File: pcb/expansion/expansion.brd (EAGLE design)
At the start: 88 x 42 mm, 53 parts, among them IC3 STM32F042F4, J1 AUDIO_JACK_3.5MM_PTH, J2 AUDIO_JACK_3.5MM_PTH, J3 AUDIO_JACK_3.5MM_PTH, J4 AUDIO_JACK_3.5MM_PTH, J5 AUDIO_JACK_3.5MM_PTH, J6 AUDIO_JACK_3.5MM_PTH, SW3 324_SW, SW4 324_SW, U1 USBC_16P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

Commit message: forgot to connect a gnd pin
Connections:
- net N$3 renamed CH1
- net N$4 renamed CH2
- net N$6 renamed CH3
- net N$7 renamed CH4
- net N$8 renamed CH5
- net N$9 renamed CH6
- net GND: now also J5.SLEEVE
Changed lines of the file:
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@@
 <grid distance="5" unitdist="mil" unit="mil" style="lines" multiple="1" display="no" altdistance="1" altunitdist="mil" altunit="mil"/>
 <layers>
-<layer number="1" name="Top" color="4" fill="1" visible="no" active="yes"/>
+<layer number="1" name="Top" color="4" fill="1" visible="yes" active="yes"/>
 <layer number="2" name="Route2" color="16" fill="1" visible="no" active="no"/>
 <layer number="3" name="Route3" color="17" fill="1" visible="no" active="no"/>
@@
 <layer number="19" name="Unrouted" color="6" fill="1" visible="yes" active="yes"/>
 <layer number="20" name="Dimension" color="24" fill="1" visible="yes" active="yes"/>
-<layer number="21" name="tPlace" color="7" fill="1" visible="no" active="yes"/>
+<layer number="21" name="tPlace" color="7" fill="1" visible="yes" active="yes"/>
 <layer number="22" name="bPlace" color="7" fill="1" visible="yes" active="yes"/>
-<layer number="23" name="tOrigins" color="15" fill="1" visible="no" active="yes"/>
+<layer number="23" name="tOrigins" color="15" fill="1" visible="yes" active="yes"/>
 <layer number="24" name="bOrigins" color="15" fill="1" visible="yes" active="yes"/>
-<layer number="25" name="tNames" color="7" fill="1" visible="no" active="yes"/>
+<layer number="25" name="tNames" color="7" fill="1" visible="yes" active="yes"/>
 <layer number="26" name="bNames" color="7" fill="1" visible="yes" active="yes"/>
-<layer number="27" name="tValues" color="7" fill="1" visible="no" active="yes"/>
-<layer number="28" name="bValues" color="7" fill="1" visible="no" active="yes"/>
+<layer number="27" name="tValues" color="7" fill="1" visible="yes" active="yes"/>
+<layer number="28" name="bValues" color="7" fill="1" visible="yes" active="yes"/>
 <layer number="29" name="tStop" color="7" fill="3" visible="no" active="yes"/>
 <layer number="30" name="bStop" color="7" fill="6" visible="no" active="yes"/>
@@
 <layer number="37" name="tTest" color="7" fill="1" visible="no" active="yes"/>
 <layer number="38" name="bTest" color="7" fill="1" visible="no" active="yes"/>
-<layer number="39" name="tKeepout" color="4" fill="11" visible="no" active="yes"/>
+<layer number="39" name="tKeepout" color="4" fill="11" visible="yes" active="yes"/>
 <layer number="40" name="bKeepout" color="1" fill="11" visible="yes" active="yes"/>
-<layer number="41" name="tRestrict" color="4" fill="10" visible="no" active="yes"/>
+<layer number="41" name="tRestrict" color="4" fill="10" visible="yes" active="yes"/>
 <layer number="42" name="bRestrict" color="1" fill="10" visible="yes" active="yes"/>
 <layer number="43" name="vRestrict" color="2" fill="10" visible="no" active="yes"/>
@@
 <layer number="49" name="Reference" color="7" fill="1" visible="no" active="yes"/>
 <layer number="50" name="dxf" color="7" fill="1" visible="no" active="no"/>
-<layer number="51" name="tDocu" color="7" fill="1" visible="no" active="yes"/>
+<layer number="51" name="tDocu" color="7" fill="1" visible="yes" active="yes"/>
 <layer number="52" name="bDocu" color="7" fill="1" visible="yes" active="yes"/>
 <layer number="53" name="tGND_GNDA" color="7" fill="1" visible="no" active="no"/>
@@
 <via x="28.194" y="23.876" extent="1-16" drill="0.5"/>
 <contactref element="R14" pad="1"/>
+<contactref element="J5" pad="SLEEVE"/>
+<wire x1="78.613" y1="28.575" x2="76.073" y2="38.227" width="0" layer="19" extent="1-1"/>
+<wire x1="81.6575" y1="25.32" x2="78.613" y2="28.575" width="0" layer="19" extent="1-1"/>
+<wire x1="80.7425" y1="24.225" x2="81.6575" y2="25.32" width="0" layer="19" extent="1-1"/>
+<wire x1="85.8375" y1="25.32" x2="81.6575" y2="25.32" width="0" layer="19" extent="1-1"/>
+<wire x1="83.693" y1="29.221" x2="81.6575" y2="25.32" width="0" layer="19" extent="1-1"/>
+<wire x1="80.7425" y1="17.775" x2="80.7425" y2="24.225" width="0" layer="19" extent="1-1"/>
+<wire x1="81.6575" y1="16.68" x2="80.7425" y2="17.775" width="0" layer="19" extent="1-1"/>
+<wire x1="85.8375" y1="16.68" x2="81.6575" y2="16.68" width="0" layer="19" extent="1-1"/>
+<wire x1="83.82" y1="12.054" x2="85.8375" y2="16.68" width="0" layer="19" extent="1-1"/>
+<wire x1="73.533" y1="13.462" x2="80.7425" y2="17.775" width="0" layer="19" extent="1-1"/>
+<wire x1="76.073" y1="3.683" x2="73.533" y2="13.462" width="0" layer="19" extent="1-1"/>
+<wire x1="61" y1="13.117" x2="73.533" y2="13.462" width="0" layer="19" extent="1-1"/>
+<wire x1="56.007" y1="15.61" x2="61" y2="13.117" width="0" layer="19" extent="1-1"/>
+<wire x1="48.387" y1="13.462" x2="56.007" y2="15.61" width="0" layer="19" extent="1-1"/>
+<wire x1="61" y1="4.917" x2="61" y2="13.117" width="0" layer="19" extent="1-1"/>
+<wire x1="53.127" y1="24.3152" x2="56.007" y2="15.61" width="0" layer="19" extent="1-1"/>
+<wire x1="53.467" y1="28.575" x2="53.127" y2="24.3152" width="0" layer="19" extent="1-1"/>
+<wire x1="48.727" y1="24.3152" x2="53.127" y2="24.3152" width="0" layer="19" extent="1-1"/>
+<wire x1="45.847" y1="22.479" x2="48.727" y2="24.3152" width="0" layer="19" extent="1-1"/>
+<wire x1="43.942" y1="22.617" x2="45.847" y2="22.479" width="0" layer="19" extent="1-1"/>
+<wire x1="61" y1="28.92" x2="53.467" y2="28.575" width="0" layer="19" extent="1-1"/>
+<wire x1="61" y1="37.12" x2="61" y2="28.92" width="0" layer="19" extent="1-1"/>
+<wire x1="35.1902" y1="21.445" x2="43.942" y2="22.617" width="0" layer="19" extent="1-1"/>
+<wire x1="32.385" y1="22.744" x2="35.1902" y2="21.445" width="0" layer="19" extent="1-1"/>
+<wire x1="28.194" y1="23.876" x2="32.385" y2="22.744" width="0" layer="19" extent="1-1"/>
+<wire x1="24.881" y1="25.527" x2="28.194" y2="23.876" width="0" layer="19" extent="1-1"/>
+<wire x1="28.321" y1="28.575" x2="24.881" y2="25.527" width="0" layer="19" extent="1-1"/>
+<wire x1="18.669" y1="23.357" x2="24.881" y2="25.527" width="0" layer="19" extent="1-1"/>
+<wire x1="15.986" y1="23.307" x2="18.669" y2="23.357" width="0" layer="19" extent="1-1"/>
+<wire x1="11.938" y1="23.357" x2="15.986" y2="23.307" width="0" layer="19" extent="1-1"/>
+<wire x1="8.1575" y1="24.225" x2="11.938" y2="23.357" width="0" layer="19" extent="1-1"/>
+<wire x1="7.2425" y1="25.32" x2="8.1575" y2="24.225" width="0" layer="19" extent="1-1"/>
+<wire x1="3.0625" y1="25.32" x2="7.2425" y2="25.32" width="0" layer="19" extent="1-1"/>
+<wire x1="5.08" y1="29.475" x2="3.0625" y2="25.32" width="0" layer="19" extent="1-1"/>
+<wire x1="10.708" y1="28.92" x2="7.2425" y2="25.32" width="0" layer="19" extent="1-1"/>
+<wire x1="8.1575" y1="17.775" x2="8.1575" y2="24.225" width="0" layer="19" extent="1-1"/>
+<wire x1="7.2425" y1="16.68" x2="8.1575" y2="17.775" width="0" layer="19" extent="1-1"/>
+<wire x1="3.0625" y1="16.68" x2="7.2425" y2="16.68" width="0" layer="19" extent="1-1"/>
+<wire x1="5.08" y1="12.562" x2="3.0625" y2="16.68" width="0" layer="19" extent="1-1"/>
+<wire x1="10.708" y1="13.117" x2="7.2425" y2="16.68" width="0" layer="19" extent="1-1"/>
+<wire x1="35.854" y1="28.92" x2="32.385" y2="22.744" width="0" layer="19" extent="1-1"/>
+<wire x1="35.854" y1="37.12" x2="35.854" y2="28.92" width="0" layer="19" extent="1-1"/>
+<wire x1="10.708" y1="37.12" x2="10.708" y2="28.92" width="0" layer="19" extent="1-1"/>
+<wire x1="10.708" y1="4.917" x2="10.708" y2="13.117" width="0" layer="19" extent="1-1"/>
+<wire x1="35.854" y1="13.117" x2="35.1902" y2="21.445" width="0" layer="19" extent="1-1"/>
+<wire x1="35.854" y1="4.917" x2="35.854" y2="13.117" width="0" layer="19" extent="1-1"/>
+<wire x1="43.434" y1="1.27" x2="35.854" y2="4.917" width="0" layer="19" extent="1-1"/>
+<wire x1="50.927" y1="3.683" x2="43.434" y2="1.27" width="0" layer="19" extent="1-1"/>
+<wire x1="50.927" y1="38.227" x2="53.467" y2="28.575" width="0" layer="19" extent="1-1"/>
+<wire x1="25.781" y1="38.227" x2="28.321" y2="28.575" width="0" layer="19" extent="1-1"/>
+<wire x1="25.781" y1="3.683" x2="35.854" y2="4.917" width="0" layer="19" extent="1-1"/>
+<wire x1="23.241" y1="13.462" x2="25.781" y2="3.683" width="0" layer="19" extent="1-1"/>
 </signal>
 <signal name="+3V3">
@@
 <wire x1="83.693" y1="23.368" x2="83.075" y2="22.75" width="0.2032" layer="1"/>
 </signal>
-<signal name="N$3">
+<signal name="CH1">
 <contactref element="J1" pad="TIP"/>
 <contactref element="JP1" pad="2"/>
@@
 <wire x1="36.449" y1="31.242" x2="25.781" y2="31.242" width="0.2032" layer="1"/>
 </signal>
-<signal name="N$4">
+<signal name="CH2">
 <contactref element="R8" pad="1"/>
 <contactref element="JP2" pad="2"/>
@@
 <wire x1="41.536" y1="29.602" x2="45.847" y2="29.602" width="0.2032" layer="1"/>
 </signal>
-<signal name="N$6">
+<signal name="CH3">
 <contactref element="R9" pad="1"/>
 <contactref element="JP3" pad="2"/>
@@
 <wire x1="66.519" y1="29.602" x2="66" y2="29.083" width="0.2032" layer="1"/>
 </signal>
-<signal name="N$7">
+<signal name="CH4">
 <contactref element="R10" pad="1"/>
 <contactref element="JP4" pad="2"/>
@@
 <wire x1="25.781" y1="11.176" x2="15.708" y2="11.176" width="0.2032" layer="1"/>
 </signal>
-<signal name="N$8">
+<signal name="CH5">
 <contactref element="R11" pad="1"/>
 <contactref element="JP5" pad="2"/>
@@
 <wire x1="40.854" y1="16.804" x2="40.8305" y2="16.8275" width="0.2032" layer="1"/>
 </signal>
-<signal name="N$9">
+<signal name="CH6">
 <contactref element="R12" pad="1"/>
 <contactref element="JP6" pad="2"/>

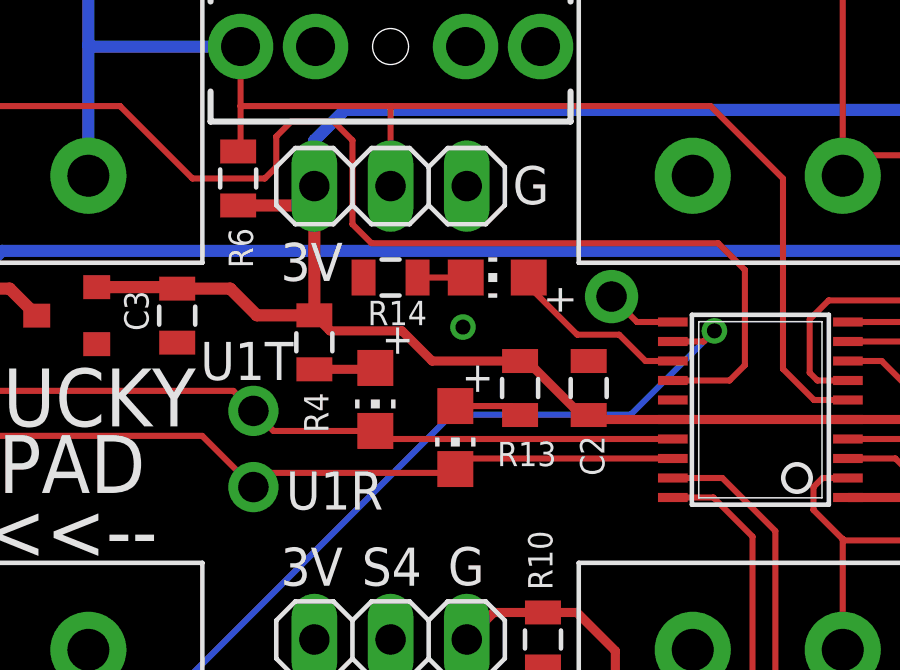
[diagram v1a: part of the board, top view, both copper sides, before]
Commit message: removed leds
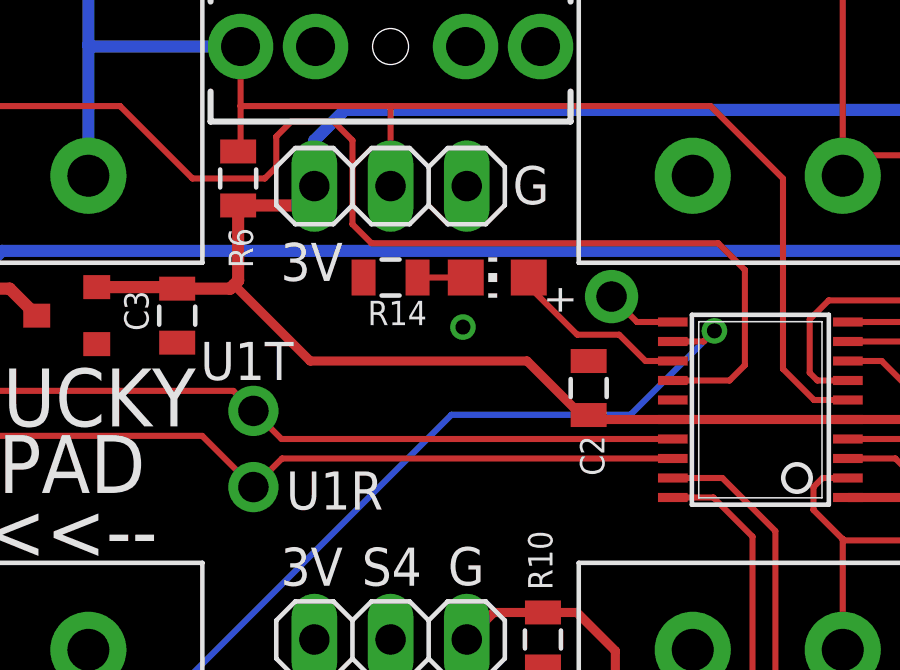
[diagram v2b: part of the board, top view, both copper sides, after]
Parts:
- removed LED1, LED2: (no value), adafruit:CHIP-LED0805
- removed R13, R4: 5.1K, SparkFun-Passives:0805
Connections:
- removed net N$10: LED2.A, R13.2
- removed net N$5: LED1.A, R4.2
- net +3V3: no longer R13.1, R4.1
- net USBDN/U1TX: no longer LED1.C
- net USBDP/U1RX: no longer LED2.C
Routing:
- net N$10: track 2.28 -> 0.00 mm
- net N$5: track 2.05 -> 0.00 mm
- net +3V3: track 224.1 -> 222.6 mm

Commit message: updated silkscreen
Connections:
- net N$13: now also J1.RING
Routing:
- net N$13: track 2.39 -> 23.7 mm, vias 0 -> 1
- net GND: track 0.00 -> 11.0 mm
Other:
- board text added: "0"
- board text added: "S1"
- board text removed: "6"
- board text removed: "S6"
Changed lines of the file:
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@@
 <text x="62.9042" y="25.1594" size="1.016" layer="25" align="center">U2RX</text>
 <text x="62.9042" y="19.3174" size="1.016" layer="25" align="center">U2TX</text>
-<text x="20.9942" y="22.7464" size="1.27" layer="25" align="center">U1T</text>
+<text x="23.9152" y="21.0954" size="1.27" layer="25" align="center">U1T</text>
 <text x="23.9152" y="18.4284" size="1.27" layer="25" align="center">U1R</text>
-<text x="3.6638" y="33.0506" size="5.08" layer="25" rot="R180" align="center">1</text>
-<text x="85.5788" y="33.1776" size="5.08" layer="25" rot="R180" align="center">3</text>
-<text x="3.6638" y="8.9206" size="5.08" layer="25" rot="R180" align="center">4</text>
-<text x="85.3248" y="8.5396" size="5.08" layer="25" rot="R180" align="center">6</text>
+<text x="63.4808" y="33.1776" size="5.08" layer="25" rot="R180" align="center">2</text>
+<text x="13.1888" y="9.0476" size="5.08" layer="25" rot="R180" align="center">3</text>
+<text x="63.6078" y="8.9206" size="5.08" layer="25" rot="R180" align="center">5</text>
 <text x="23.1532" y="26.0484" size="1.27" layer="25" align="center">3V</text>
 <text x="30.4608" y="28.6056" size="1.27" layer="25" rot="R180" align="center">G</text>
 <text x="23.1532" y="15.8884" size="1.27" layer="25" align="center">3V</text>
 <text x="28.3018" y="15.9056" size="1.27" layer="25" rot="R180" align="center">G</text>
-<text x="25.8202" y="15.8884" size="1.27" layer="25" align="center">S4</text>
+<text x="25.8202" y="15.8884" size="1.27" layer="25" align="center">S3</text>
 <text x="48.1722" y="15.8884" size="1.27" layer="25" align="center">3V</text>
-<text x="50.8392" y="15.8884" size="1.27" layer="25" align="center">S5</text>
+<text x="50.8392" y="15.8884" size="1.27" layer="25" align="center">S4</text>
 <text x="53.4478" y="26.1926" size="1.27" layer="25" rot="R180" align="center">G</text>
 <text x="73.4452" y="16.0154" size="1.27" layer="25" align="center">3V</text>
-<text x="75.9852" y="16.0154" size="1.27" layer="25" align="center">S6</text>
+<text x="75.9852" y="16.0154" size="1.27" layer="25" align="center">S5</text>
 <text x="78.5938" y="16.0326" size="1.27" layer="25" rot="R180" align="center">G</text>
 <text x="48.4262" y="26.1754" size="1.27" layer="25" align="center">3V</text>
 <text x="73.5722" y="26.0484" size="1.27" layer="25" align="center">3V</text>
 <text x="78.7208" y="26.0656" size="1.27" layer="25" rot="R180" align="center">G</text>
-<text x="76.1122" y="26.0484" size="1.27" layer="25" align="center">S3</text>
-<text x="50.9662" y="26.1754" size="1.27" layer="25" align="center">S2</text>
+<text x="76.1122" y="26.0484" size="1.27" layer="25" align="center">S2</text>
+<text x="50.9662" y="26.1754" size="1.27" layer="25" align="center">S1</text>
 <text x="53.4478" y="15.9056" size="1.27" layer="25" rot="R180" align="center">G</text>
 <text x="15.1568" y="19.3106" size="1.9304" layer="25" distance="15" rot="R180" align="center">DUCKY
@@
 PAD
 &lt;&lt;--</text>
-<text x="13.1888" y="33.4316" size="5.08" layer="26" rot="MR180" align="center">1</text>
-<text x="38.3348" y="33.3046" size="5.08" layer="26" rot="MR180" align="center">2</text>
-<text x="63.4808" y="33.1776" size="5.08" layer="26" rot="MR180" align="center">3</text>
-<text x="13.1888" y="9.0476" size="5.08" layer="26" rot="MR180" align="center">4</text>
-<text x="38.3348" y="8.9206" size="5.08" layer="26" rot="MR180" align="center">5</text>
-<text x="63.4808" y="8.9206" size="5.08" layer="26" rot="MR180" align="center">6</text>
-<text x="15.5378" y="20.8346" size="1.9304" layer="26" distance="15" rot="MR180" align="center">DUCKY
+<text x="13.1888" y="33.4316" size="5.08" layer="26" rot="MR180" align="center">0</text>
+<text x="38.3348" y="33.3046" size="5.08" layer="26" rot="MR180" align="center">1</text>
+<text x="63.4808" y="33.1776" size="5.08" layer="26" rot="MR180" align="center">2</text>
+<text x="13.1888" y="9.0476" size="5.08" layer="26" rot="MR180" align="center">3</text>
+<text x="38.3348" y="8.9206" size="5.08" layer="26" rot="MR180" align="center">4</text>
+<text x="63.4808" y="8.9206" size="5.08" layer="26" rot="MR180" align="center">5</text>
+<text x="14.7758" y="20.7076" size="1.9304" layer="26" distance="15" rot="MR180" align="center">DUCKY
 PAD
 ---&gt;&gt;</text>
+<text x="38.4618" y="33.3046" size="5.08" layer="25" rot="R180" align="center">1</text>
+<text x="38.3348" y="8.9206" size="5.08" layer="25" rot="R180" align="center">4</text>
+<text x="13.1888" y="33.4316" size="5.08" layer="25" rot="R180" align="center">0</text>
 </plain>
 <attributes>
@@
 <element name="U2" library="my_usbc_16p" package="USBC_16P_FOOT" value="USBC_16P" x="4.31" y="21" smashed="yes" rot="R270"/>
 <element name="R1" library="joyAnalog" package="0805" value="5.1K" x="5.08" y="13.462" smashed="yes" rot="R270">
-<attribute name="NAME" x="6.5778" y="13.0556" size="0.8128" layer="25" rot="R90"/>
+<attribute name="NAME" x="5.4348" y="10.7696" size="0.8128" layer="25" rot="R90"/>
 </element>
 <element name="R2" library="joyAnalog" package="0805" value="5.1K" x="5.08" y="28.575" smashed="yes" rot="R90">
@@
 </element>
 <element name="C1" library="clock" package="0805" value="1uF" x="11.938" y="24.257" smashed="yes" rot="R90">
-<attribute name="NAME" x="10.2235" y="25.3238" size="0.8128" layer="25" rot="R270"/>
+<attribute name="NAME" x="10.0965" y="25.3238" size="0.8128" layer="25" rot="R270"/>
 </element>
 <element name="IC3" library="tx" package="TSSOP20" value="STM32F042F4" x="38.108" y="21.12" smashed="yes" rot="R90"/>
@@
 <element name="SW4" library="3pos_slide_switch_centered" package="342_SWICH_FOOT" value="324_SW" x="50.927" y="19.05" smashed="yes" rot="R180"/>
 <element name="R5" library="joyAnalog" package="0805" value="10K" x="56.007" y="16.51" smashed="yes" rot="R90">
-<attribute name="NAME" x="55.5155" y="14.8374" size="0.8128" layer="25" rot="R270"/>
+<attribute name="NAME" x="56.9125" y="17.5044" size="0.8128" layer="25" rot="R270"/>
 </element>
 <element name="U4" library="3pos_slide_switch" package="SOT23R_INFINEON" value="XC6206_DEV" x="14.986" y="24.257" smashed="yes" rot="R90"/>
@@
 </element>
 <element name="R11" library="joyAnalog" package="0805" value="10K" x="56.007" y="13.462" smashed="yes" rot="R90">
-<attribute name="NAME" x="57.7215" y="14.097" size="0.8128" layer="25" rot="R270"/>
+<attribute name="NAME" x="58.3565" y="12.573" size="0.8128" layer="25" rot="R90"/>
 </element>
 <element name="R12" library="joyAnalog" package="0805" value="10K" x="81.407" y="12.954" smashed="yes" rot="R90">
@@
 <contactref element="R14" pad="1"/>
 <contactref element="J5" pad="SLEEVE"/>
+<wire x1="35.854" y1="28.92" x2="38.1" y2="26.674" width="0.254" layer="1"/>
+<wire x1="37.574" y1="21.445" x2="35.1902" y2="21.445" width="0.254" layer="1"/>
+<wire x1="38.1" y1="26.674" x2="38.1" y2="21.971" width="0.254" layer="1"/>
+<wire x1="38.1" y1="21.971" x2="37.574" y2="21.445" width="0.254" layer="1"/>
 </signal>
 <signal name="+3V3">
@@
 <contactref element="IC3" pad="6"/>
 <wire x1="41.0258" y1="21.445" x2="39.896" y2="21.445" width="0.2032" layer="1"/>
-<wire x1="39.896" y1="21.445" x2="38.862" y2="22.479" width="0.2032" layer="1"/>
+<wire x1="39.896" y1="21.445" x2="38.608" y2="22.733" width="0.2032" layer="1"/>
 <wire x1="20.781" y1="33.227" x2="20.781" y2="31.242" width="0.2032" layer="1"/>
 <wire x1="20.781" y1="31.242" x2="20.781" y2="29.809" width="0.2032" layer="1"/>
@@
 <wire x1="25.781" y1="31.242" x2="20.781" y2="31.242" width="0.2032" layer="1"/>
 <wire x1="25.781" y1="28.575" x2="25.781" y2="31.242" width="0.2032" layer="1"/>
-<wire x1="38.862" y1="22.479" x2="38.862" y2="28.829" width="0.2032" layer="1"/>
-<wire x1="38.862" y1="28.829" x2="36.449" y2="31.242" width="0.2032" layer="1"/>
+<wire x1="38.608" y1="22.733" x2="38.608" y2="29.083" width="0.2032" layer="1"/>
+<wire x1="38.608" y1="29.083" x2="36.449" y2="31.242" width="0.2032" layer="1"/>
 <wire x1="36.449" y1="31.242" x2="25.781" y2="31.242" width="0.2032" layer="1"/>
 </signal>
@@
 <wire x1="35.1902" y1="22.745" x2="34.278" y2="22.745" width="0.2032" layer="1"/>
 <wire x1="30.387" y1="25.239" x2="30.387" y2="25.527" width="0.2032" layer="1"/>
-<wire x1="34.278" y1="22.745" x2="33.401" y2="23.622" width="0.2032" layer="1"/>
-<wire x1="33.401" y1="23.622" x2="32.004" y2="23.622" width="0.2032" layer="1"/>
-<wire x1="32.004" y1="23.622" x2="30.387" y2="25.239" width="0.2032" layer="1"/>
+<wire x1="34.278" y1="22.745" x2="33.4518" y2="23.5712" width="0.2032" layer="1"/>
+<wire x1="33.4518" y1="23.5712" x2="32.0548" y2="23.5712" width="0.2032" layer="1"/>
+<wire x1="32.0548" y1="23.5712" x2="30.387" y2="25.239" width="0.2032" layer="1"/>
 </signal>
 <signal name="N$13">
@@
 <wire x1="35.1902" y1="24.045" x2="33.994" y2="24.045" width="0.2032" layer="1"/>
 <wire x1="33.994" y1="24.045" x2="33.147" y2="24.892" width="0.2032" layer="1"/>
+<contactref element="J1" pad="RING"/>
+<wire x1="33.147" y1="24.892" x2="33.528" y2="25.273" width="0.2032" layer="16"/>
+<wire x1="39.497" y1="25.273" x2="39.624" y2="25.4" width="0.2032" layer="16"/>
+<wire x1="39.497" y1="25.273" x2="33.528" y2="25.273" width="0.2032" layer="16"/>
+<via x="39.624" y="25.4" extent="1-16" drill="0.5"/>
+<wire x1="39.624" y1="25.4" x2="39.116" y2="25.908" width="0.2032" layer="1"/>
+<wire x1="36.115" y1="33.227" x2="30.781" y2="33.227" width="0.2032" layer="1"/>
+<wire x1="39.116" y1="25.908" x2="39.116" y2="30.226" width="0.2032" layer="1"/>
+<wire x1="39.116" y1="30.226" x2="36.115" y2="33.227" width="0.2032" layer="1"/>
 </signal>
 <signal name="N$14">
